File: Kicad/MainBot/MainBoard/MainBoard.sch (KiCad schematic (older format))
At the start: 33 parts, among them U1 AZ1117-3.3, U2 Teensy3.6

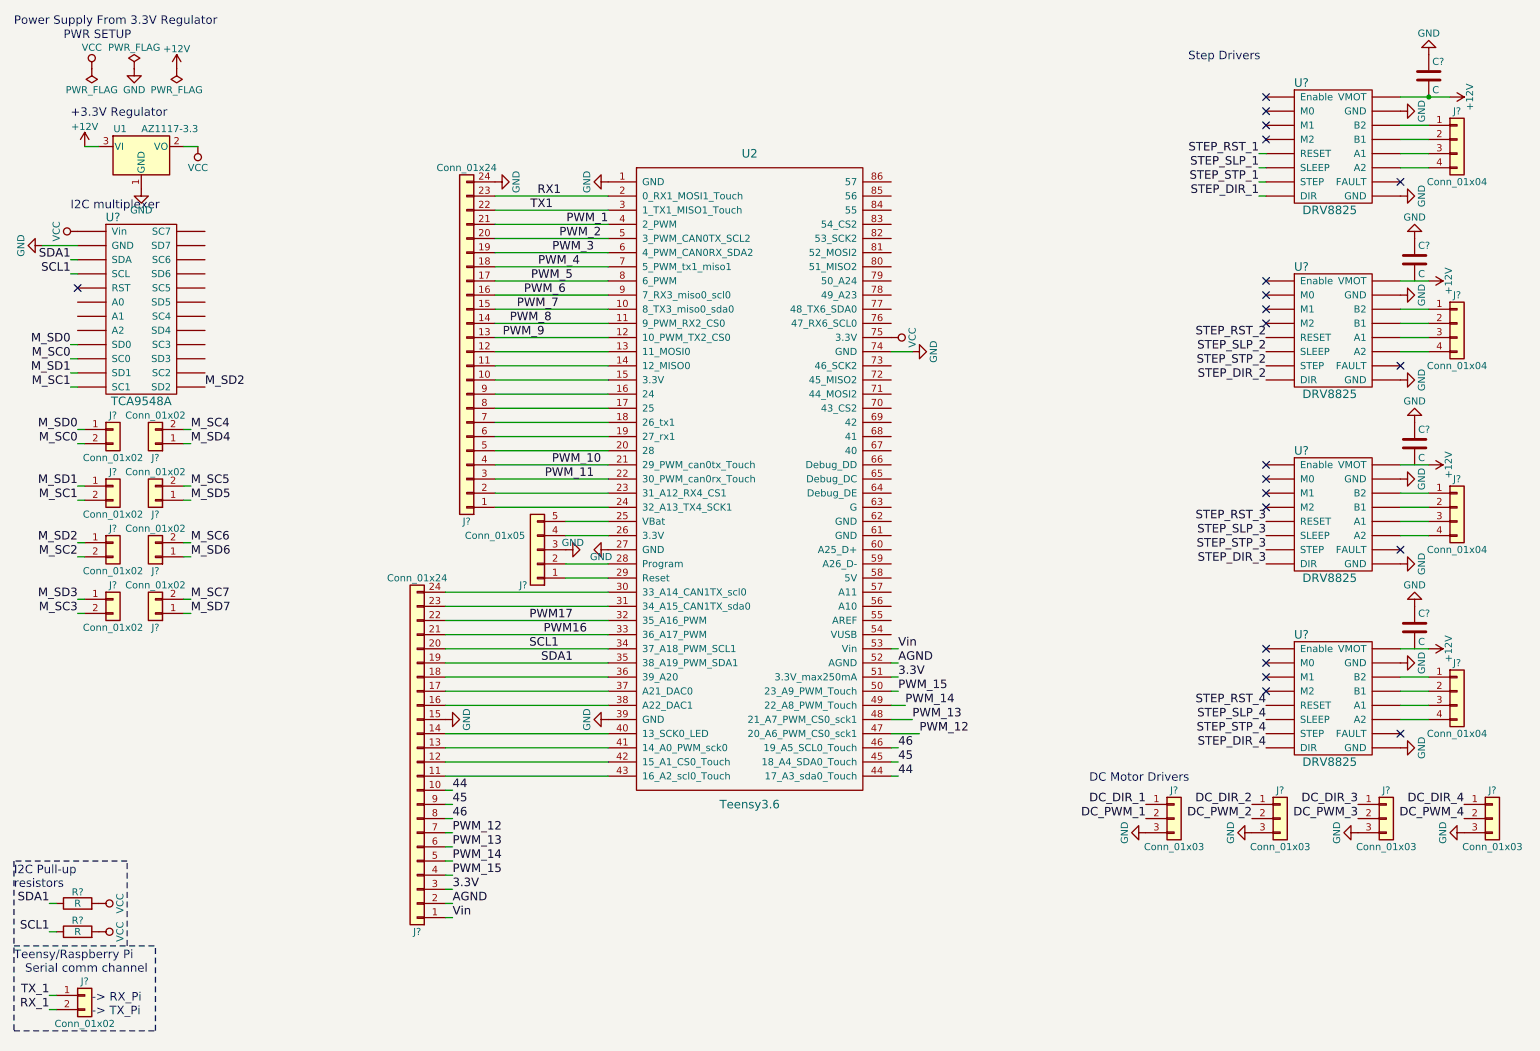
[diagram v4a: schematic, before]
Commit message: Added multiplexer and driver footprint, updated PCB
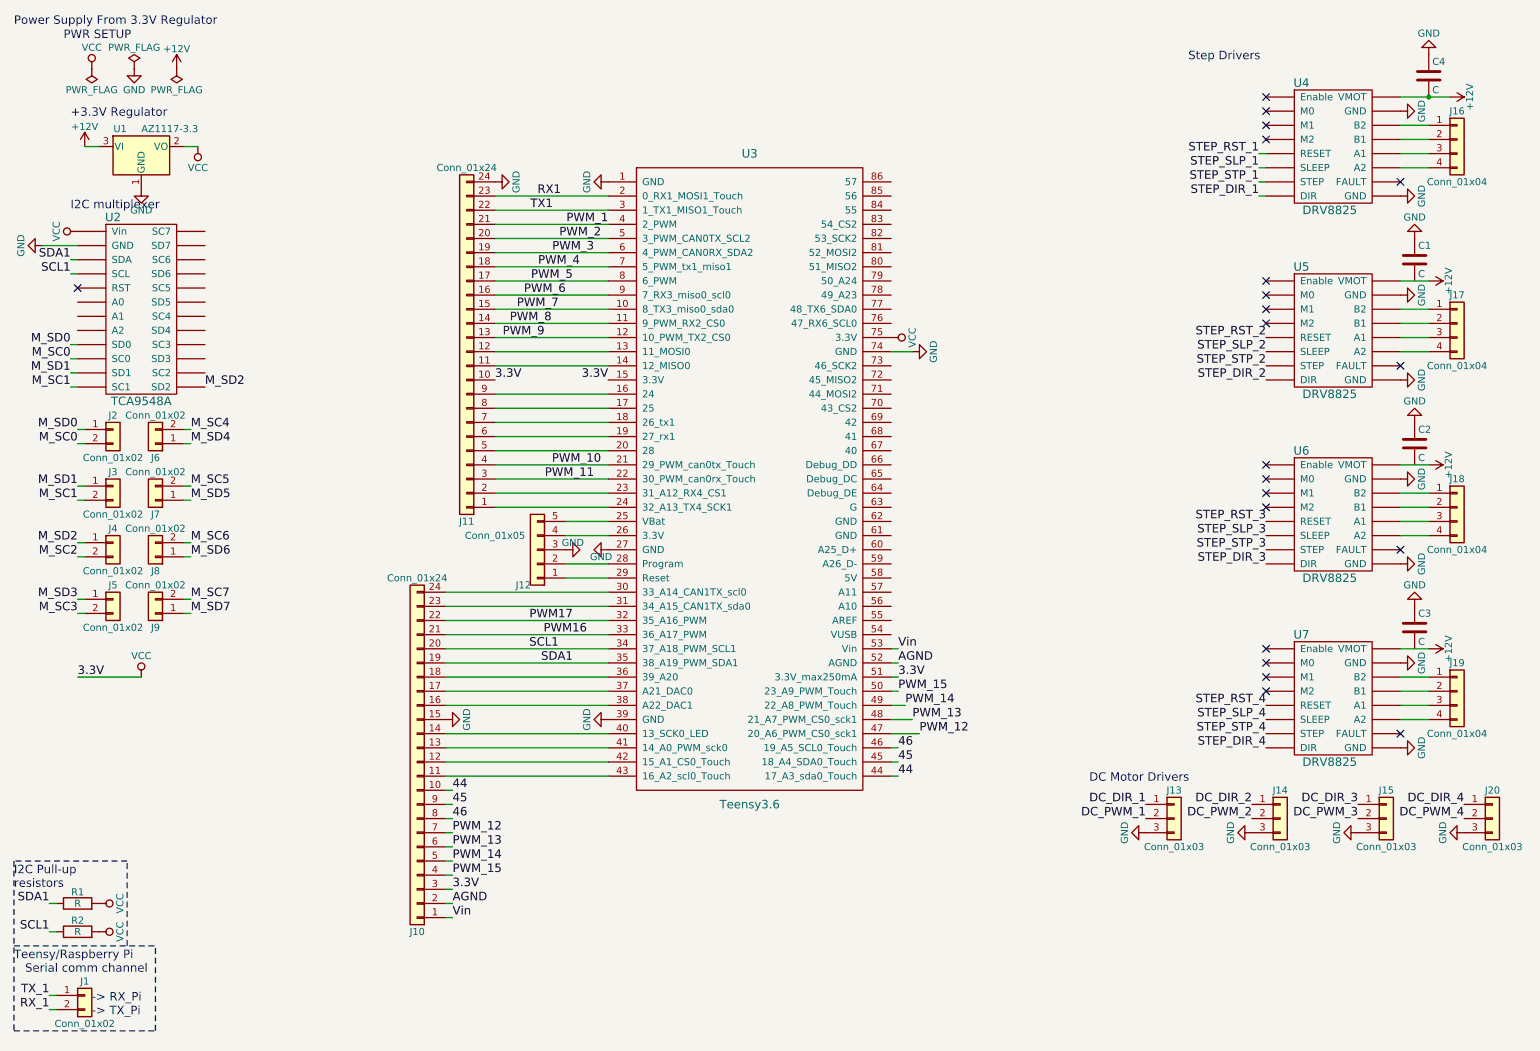
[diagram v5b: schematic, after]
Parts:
- C1, C2, C3, C4: renamed from C?; footprint (none) -> Capacitors_THT:C_Disc_D4.7mm_W2.5mm_P5.00mm
- J1, J2, J3, J4, J5, J6, J7, J8, J9: renamed from J?; footprint (none) -> Pin_Headers:Pin_Header_Straight_1x02_Pitch2.00mm
- J10, J11: renamed from J?; footprint (none) -> Pin_Headers:Pin_Header_Straight_1x24_Pitch2.54mm
- J12: renamed from J?; footprint (none) -> Pin_Headers:Pin_Header_Straight_1x05_Pitch2.54mm
- J13, J14, J15, J20: renamed from J?; footprint (none) -> Pin_Headers:Pin_Header_Straight_1x03_Pitch2.54mm
- J16, J17, J18, J19: renamed from J?; footprint (none) -> Pin_Headers:Pin_Header_Straight_1x04_Pitch2.54mm
- R1, R2: renamed from R?; footprint (none) -> Resistors_THT:R_Axial_DIN0207_L6.3mm_D2.5mm_P7.62mm_Horizontal
- U2: renamed from U?; footprint (none) -> Rex:TCA9548A
- U4, U5, U6, U7: renamed from U?; footprint (none) -> Rex:DRV8825
- renumbered U2 to U3
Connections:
- net 3.3V is gone; now on net VCC: J10.3 (Pin_3), U3.51 (3.3V_max250mA)
- net VCC: now also J11.10 (Pin_10), U3.15 (3.3V)

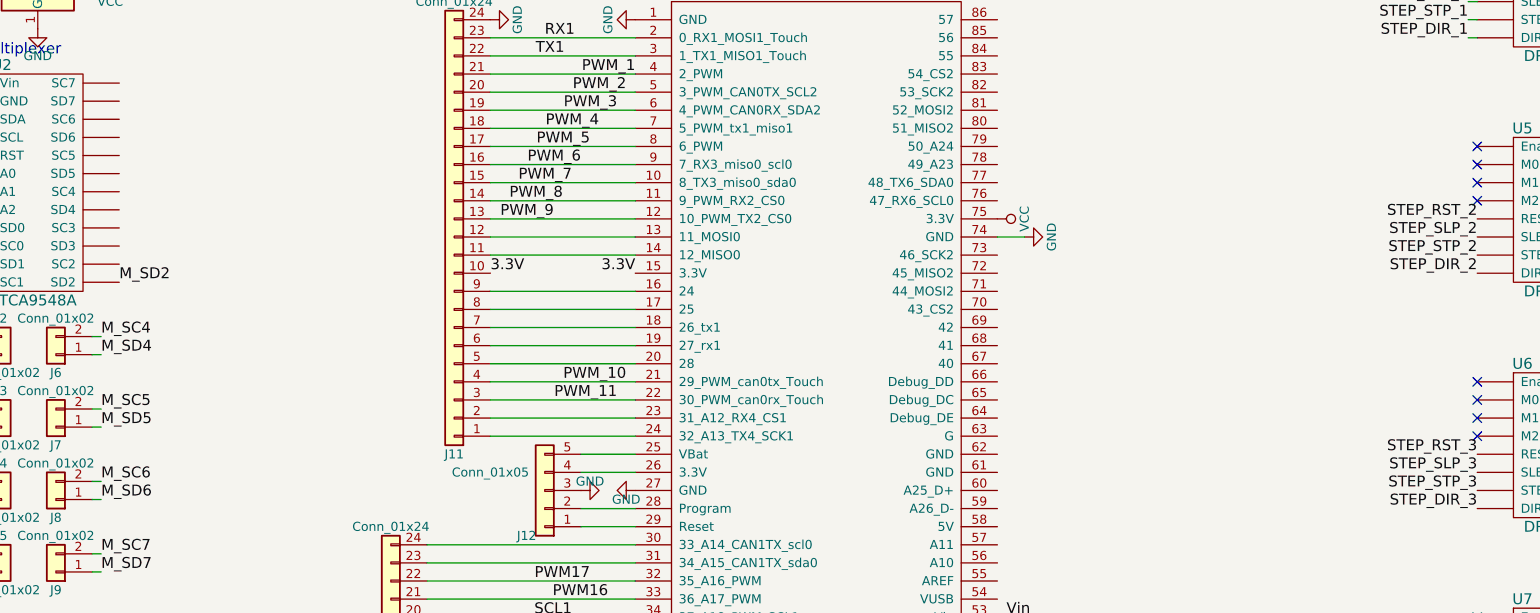
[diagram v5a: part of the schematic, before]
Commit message: Added notes on schematic
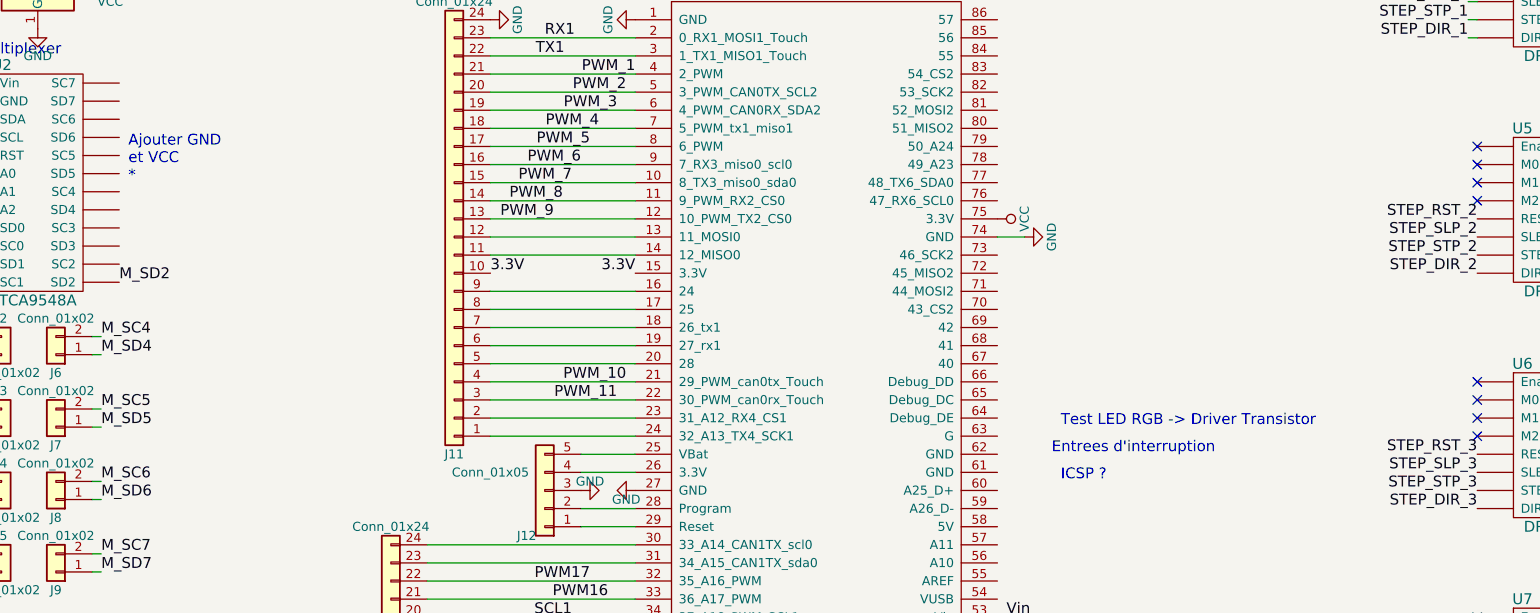
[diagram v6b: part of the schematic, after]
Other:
- note added: "Ajouter GND \net VCC\n*"
- note added: "Entrees d'interruption\n"
- note added: "ICSP ?\n"
- note added: "Test LED RGB -> Driver Transistor\n"
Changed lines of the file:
@@
 Wire Wire Line
 	950  5250 1400 5250
+Text Notes 1900 2650 0    60   ~ 0
+Ajouter GND \net VCC\n*
+Text Notes 7000 4150 0    60   ~ 0
+Entrees d'interruption\n
+Text Notes 7050 4300 0    60   ~ 0
+ICSP ?\n
+Text Notes 7050 4000 0    60   ~ 0
+Test LED RGB -> Driver Transistor\n
 $EndSCHEMATC

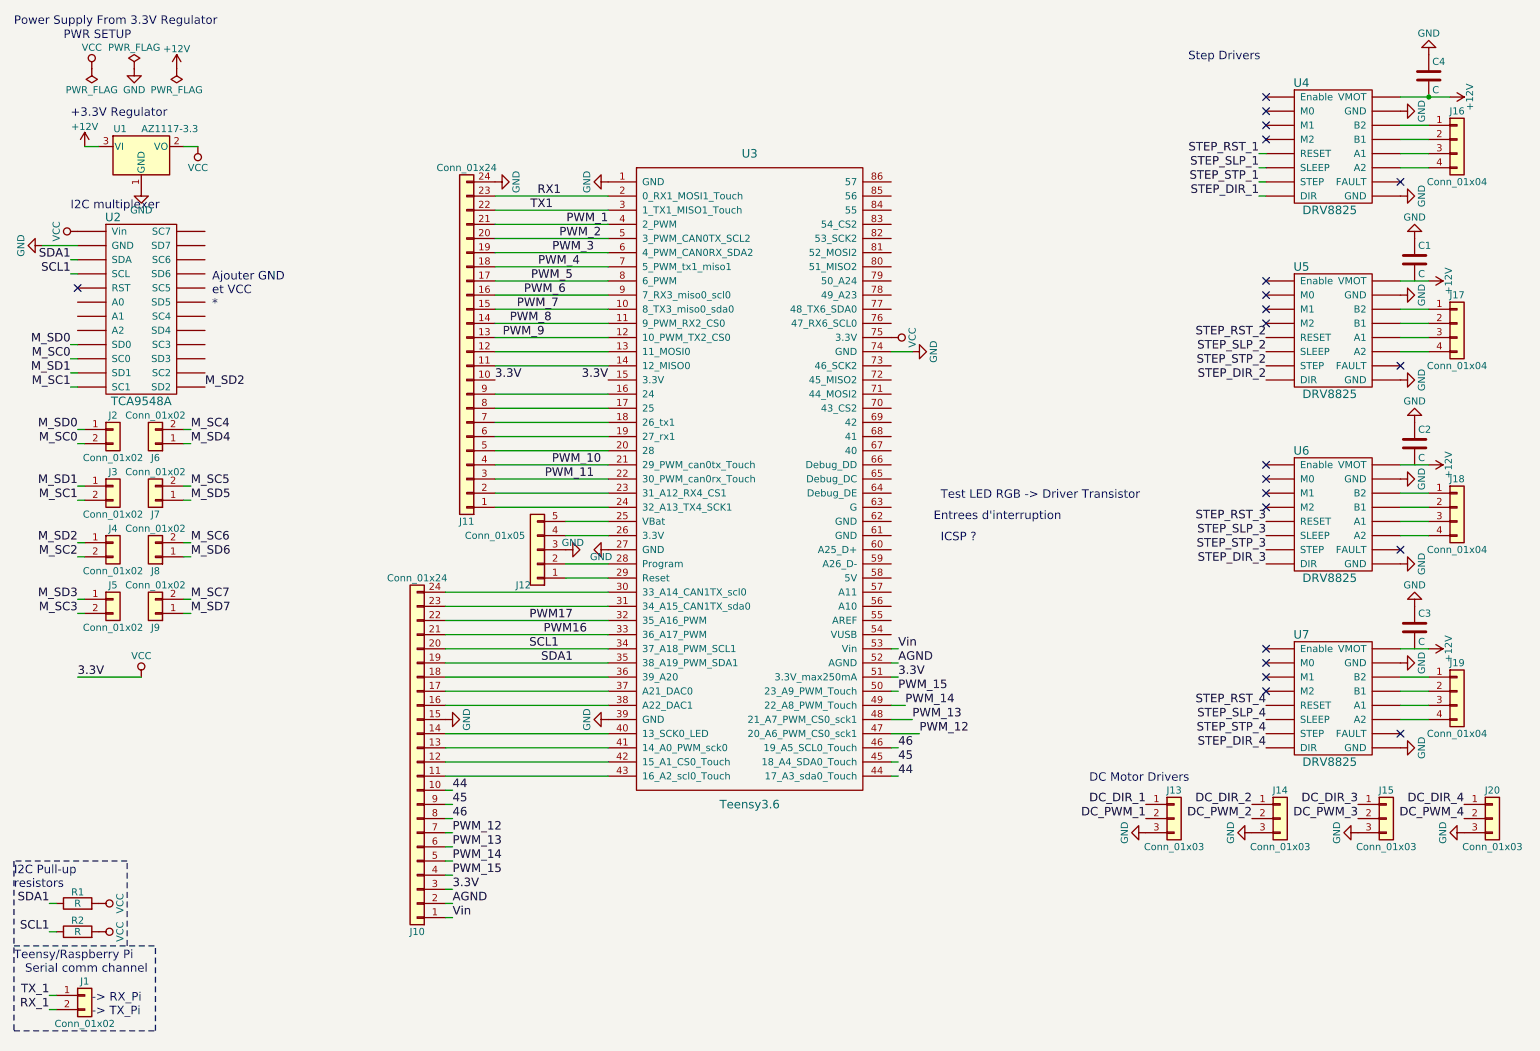
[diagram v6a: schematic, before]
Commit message: Added capacitors to regulator, ICSP2 pins, completed I2C Vcc and GND connections
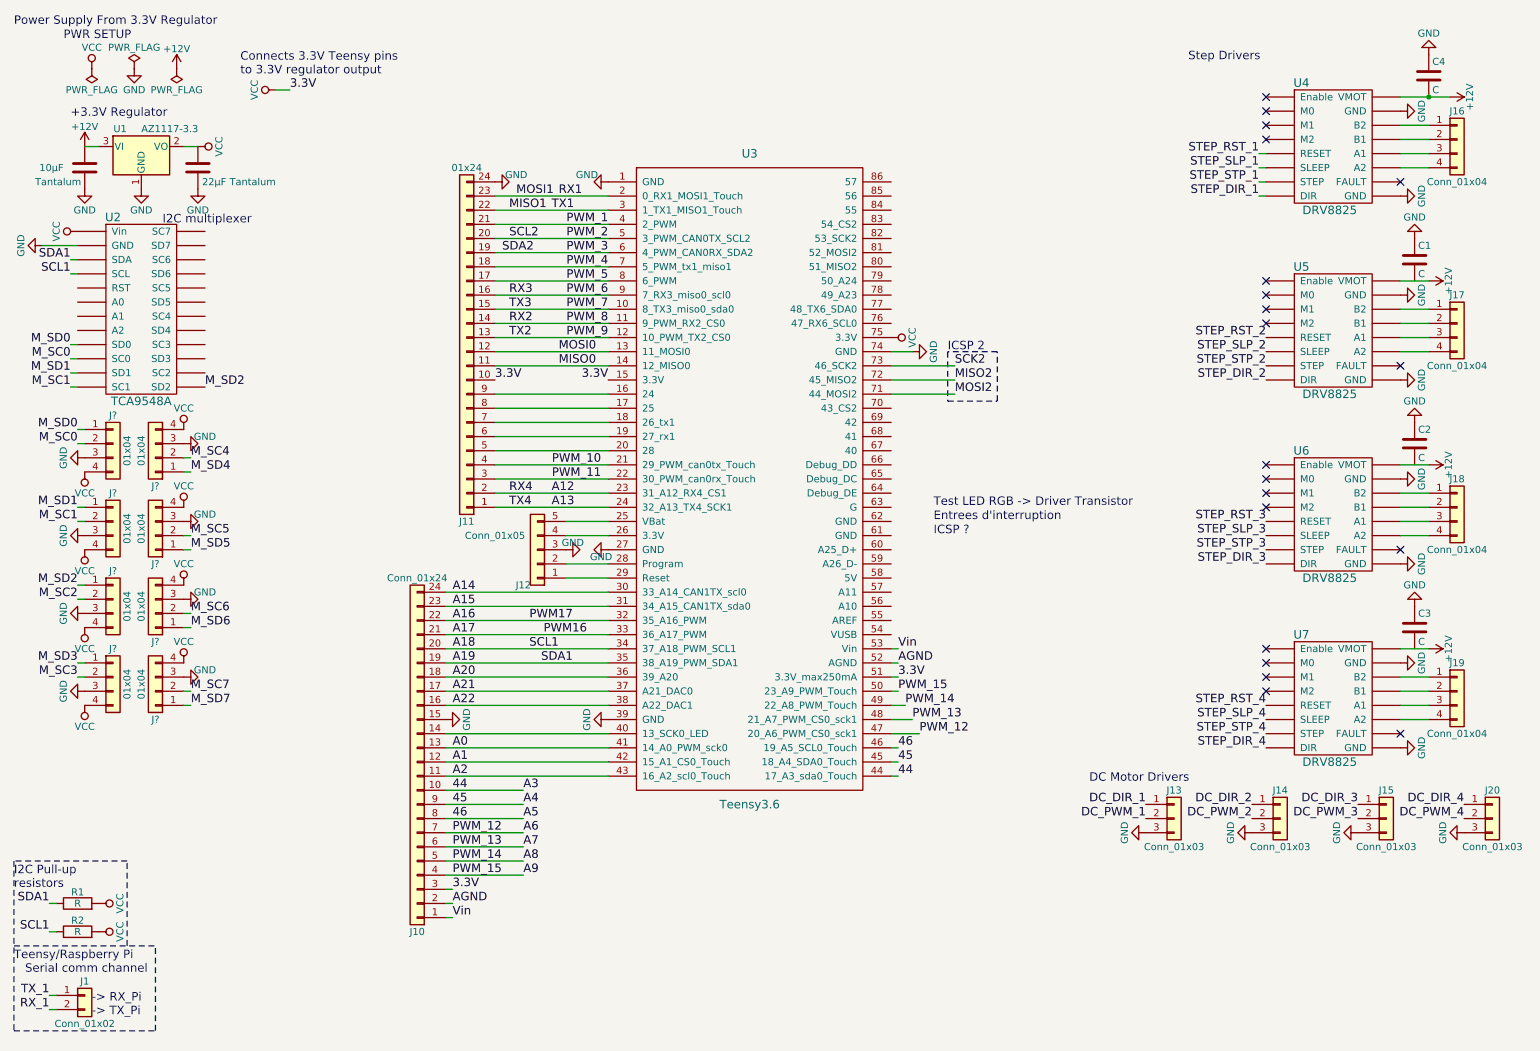
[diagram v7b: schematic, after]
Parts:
- removed J2, J3, J4, J5, J6, J7, J8, J9: Conn_01x02, Pin_Headers:Pin_Header_Straight_1x02_Pitch2.00mm, symbol Conn_01x02
- added J? (x8): 01x04, symbol Conn_01x04
- added Tantalum: 10µF, symbol C
- added Tantalum: 22µF, symbol C
- J11: value Conn_01x24 -> 01x24
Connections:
- net +12V: now also Tantalum.2
- net GND: now also J?.3 (Pin_3), J?.3 (Pin_3), J?.3 (Pin_3), J?.3 (Pin_3), J?.3 (Pin_3), J?.3 (Pin_3), J?.3 (Pin_3), J?.3 (Pin_3), Tantalum.1, Tantalum.1
- net M_SC0: now also J?.2 (Pin_2)
- net M_SC1: now also J?.2 (Pin_2)
- net M_SC2: now also J?.2 (Pin_2)
- net M_SC3: now also J?.2 (Pin_2)
- net M_SC4: now also J?.2 (Pin_2)
- net M_SC5: now also J?.2 (Pin_2)
- net M_SC6: now also J?.2 (Pin_2)
- net M_SC7: now also J?.2 (Pin_2)
- net M_SD0: now also J?.1 (Pin_1)
- net M_SD1: now also J?.1 (Pin_1)
- net M_SD2: now also J?.1 (Pin_1)
- net M_SD3: now also J?.1 (Pin_1)
- net M_SD4: now also J?.1 (Pin_1)
- net M_SD5: now also J?.1 (Pin_1)
- net M_SD6: now also J?.1 (Pin_1)
- net M_SD7: now also J?.1 (Pin_1)
- net VCC: now also J?.4 (Pin_4), J?.4 (Pin_4), J?.4 (Pin_4), J?.4 (Pin_4), J?.4 (Pin_4), J?.4 (Pin_4), J?.4 (Pin_4), J?.4 (Pin_4), Tantalum.2
- net MOSI0: now reaches J11.12 (Pin_12), U3.13 (11_MOSI0)
- net MISO0: now reaches J11.11 (Pin_11), U3.14 (12_MISO0)
- net A12: now reaches J11.2 (Pin_2), U3.23 (31_A12_RX4_CS1)
- net A13: now reaches J11.1 (Pin_1), U3.24 (32_A13_TX4_SCK1)
- net A14: now reaches J10.24 (Pin_24), U3.30 (33_A14_CAN1TX_scl0)
- net A15: now reaches J10.23 (Pin_23), U3.31 (34_A15_CAN1TX_sda0)
- net A20: now reaches J10.18 (Pin_18), U3.36 (39_A20)
- net A21: now reaches J10.17 (Pin_17), U3.37 (A21_DAC0)
- net A22: now reaches J10.16 (Pin_16), U3.38 (A22_DAC1)
- net A0: now reaches J10.13 (Pin_13), U3.41 (14_A0_PWM_sck0)
- net A1: now reaches J10.12 (Pin_12), U3.42 (15_A1_CS0_Touch)
- net A2: now reaches J10.11 (Pin_11), U3.43 (16_A2_scl0_Touch)
- net MOSI2: now reaches U3.71 (44_MOSI2)
- net MISO2: now reaches U3.72 (45_MISO2)
- net SCK2: now reaches U3.73 (46_SCK2)
- net PWM16 renamed A17
- net PWM17 renamed A16
- net PWM_12 renamed A6
- net PWM_13 renamed A7
- net PWM_14 renamed A8
- net PWM_15 renamed A9
- net RX1 renamed MOSI1
- net SCL1 renamed A18
- net SDA1 renamed A19
- net TX1 renamed MISO1
- no-connect marks 21 -> 20
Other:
- note added: "Connects 3.3V Teensy pins \nto 3.3V regulator output"
- note added: "ICSP 2\n"
- note removed: "Ajouter GND \net VCC\n*"
